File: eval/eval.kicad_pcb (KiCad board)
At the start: 2 copper layers, 2 parts, among them U1 STM32G031G8U6, U2 LM5148RGYR

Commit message: [Layout] complete loop, root and buck layout
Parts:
- added C1: 100n, Capacitor_SMD:C_0603_1608Metric, F.Cu at (77.9, 133.6)
- added C10: 10n, Capacitor_SMD:C_0603_1608Metric, F.Cu at (131.2, 126.4)
- added C11: 10n, Capacitor_SMD:C_0603_1608Metric, F.Cu at (64.9, 175.4)
- added C12: 10n, Capacitor_SMD:C_0603_1608Metric, F.Cu at (135.1, 128.5)
- added C13: 15n, Capacitor_SMD:C_0603_1608Metric, F.Cu at (74.5, 179.3)
- added C14: 100n, Capacitor_SMD:C_0603_1608Metric, F.Cu at (1758.3, 58.4)
- added C15: 15n, Capacitor_SMD:C_0603_1608Metric, F.Cu at (74.5, 176.2)
- added C16: 100n, Capacitor_SMD:C_0603_1608Metric, F.Cu at (1702.5, 61.0)
- added C17: 10n, Capacitor_SMD:C_0603_1608Metric, F.Cu at (69.4, 115.2)
- added C18: 10n, Capacitor_SMD:C_0603_1608Metric, F.Cu at (65.8, 113.5)
- added C19: 1u, Capacitor_SMD:C_0603_1608Metric, F.Cu at (59.2, 84.7)
- added C2: 2.2u, Capacitor_SMD:C_0603_1608Metric, F.Cu at (77.8, 142.0)
- added C20: 4.7u, Capacitor_SMD:C_0603_1608Metric, F.Cu at (59.2, 81.6)
- added C21: 100n, Capacitor_SMD:C_0603_1608Metric, F.Cu at (59.2, 83.1)
- added C22: 100n, Capacitor_SMD:C_0603_1608Metric, F.Cu at (1708.8, 61.0)
- added C23: 22uf, Capacitor_SMD:C_0603_1608Metric, F.Cu at (1790.1, 63.5)
- added C24: 22uf, Capacitor_SMD:C_0603_1608Metric, F.Cu at (1799.0, 63.5)
- added C25: 75p, Capacitor_SMD:C_0603_1608Metric, F.Cu at (1767.2, 73.7)
- added C26: 1u, Capacitor_SMD:C_0603_1608Metric, F.Cu at (1702.5, 121.9)
- added C27: 1u, Capacitor_SMD:C_0603_1608Metric, F.Cu at (1778.7, 121.9)
- added C28: 1u, Capacitor_SMD:C_0603_1608Metric, F.Cu at (1749.4, 123.2)
- added C29: 1u, Capacitor_SMD:C_0603_1608Metric, F.Cu at (1829.5, 123.2)
- added C30: 1u, Capacitor_SMD:C_0603_1608Metric, F.Cu at (1438.6, 119.4)
- added C31: 100p, Capacitor_SMD:C_0603_1608Metric, F.Cu at (1479.3, 142.2)
- added C32: 100p, Capacitor_SMD:C_0603_1608Metric, F.Cu at (1391.6, 128.3)
- added C33: 100, Capacitor_SMD:C_0603_1608Metric, F.Cu at (77.7, 140.5)
- added C36: 10u, EasyEDA:C1206, F.Cu at (88.6, 123.7)
- added C37: 10u, EasyEDA:C1206, F.Cu at (85.2, 123.7)
- added C38: 100n, Capacitor_SMD:C_0603_1608Metric, F.Cu at (64.2, 177.8)
- added C40: 47u, EasyEDA:C1206, F.Cu at (120.3, 140.4)
- added C41: 47u, EasyEDA:C1206, F.Cu at (117.0, 140.4)
- added C42: 47u, EasyEDA:C1206, F.Cu at (113.6, 140.4)
- added C43: 47u, EasyEDA:C1206, F.Cu at (110.3, 140.4)
- added C7: 100n, Capacitor_SMD:C_0603_1608Metric, F.Cu at (75.4, 141.2)
- added C8: 10u, EasyEDA:C1206, F.Cu at (95.2, 123.7)
- added C9: 10u, EasyEDA:C1206, F.Cu at (91.9, 123.7)
- added D1: BAT54,215, EasyEDA:SOT-23_L2.9-W1.3-P1.90-LS2.4-BR, F.Cu at (64.9, 171.6)
- added D2: BDFN2A301V35, EasyEDA:DFN1006-2L-RD, F.Cu at (1134.2, 100.3)
- added D3: BDFN2A301V35, EasyEDA:DFN1006-2L-RD, F.Cu at (1140.5, 100.3)
- added D6: SMAJ20A_C41376408, EasyEDA:SMA_L4.3-W2.6-LS5.2-RD, F.Cu at (1154.5, 100.3)
- added J1: TC2030, Connector:Tag-Connect_TC2030-IDC-NL_2x03_P1.27mm_Vertical, F.Cu at (76.2, 78.0)
- added L1: SMIS130804-R47MT, EasyEDA:IND-SMD_L12.8-W7.8, F.Cu at (99.3, 137.4)
- added Q1: BSC0702LS, EasyEDA:PG-TDSON-8_L5.0-W6.0-P1.27-BL-EP, F.Cu at (86.6, 133.1)
- added Q2: BSC0702LS, EasyEDA:PG-TDSON-8_L5.0-W6.0-P1.27-BL-EP, F.Cu at (86.6, 143.1)
- added Q3: AP40P04G, EasyEDA:PDFN-8_L5.8-W4.9-P1.27-LS6.1-BL-A, F.Cu at (1215.5, 52.1)
- added Q4: DMG2302UK-7, EasyEDA:SOT-23-3_L2.9-W1.3-P1.90-LS2.4-BR, F.Cu at (1410.7, 125.7)
- added R1: RE2512F3R010, EasyEDA:R2512, F.Cu at (69.3, 121.9)
- added R10: R_Small, Resistor_SMD:R_0603_1608Metric, F.Cu at (64.2, 179.3)
- added R11: 10k, Resistor_SMD:R_0603_1608Metric, F.Cu at (61.0, 176.2)
- added R12: 100k, Resistor_SMD:R_0603_1608Metric, F.Cu at (63.3, 175.4)
- added R13: 10, Resistor_SMD:R_0603_1608Metric, F.Cu at (134.2, 130.8)
- added R14: 10, Resistor_SMD:R_0603_1608Metric, F.Cu at (135.9, 130.8)
- added R15: 1k, Resistor_SMD:R_0603_1608Metric, F.Cu at (77.0, 180.1)
- added R16: 49.9, Resistor_SMD:R_0603_1608Metric, F.Cu at (1776.1, 64.8)
- added R17: 100, Resistor_SMD:R_0603_1608Metric, F.Cu at (71.6, 181.4)
- added R18: 1k, Resistor_SMD:R_0603_1608Metric, F.Cu at (76.9, 175.5)
- added R19: 100k, Resistor_SMD:R_0603_1608Metric, F.Cu at (1776.1, 72.4)
- added R2: 100k, Resistor_SMD:R_0603_1608Metric, F.Cu at (73.8, 130.4)
- added R20: 100, Resistor_SMD:R_0603_1608Metric, F.Cu at (71.6, 173.8)
- added R21: 10, Resistor_SMD:R_0603_1608Metric, F.Cu at (68.7, 117.6)
- added R22: 10, Resistor_SMD:R_0603_1608Metric, F.Cu at (70.2, 117.7)
- added R23: 1k, Resistor_SMD:R_0603_1608Metric, F.Cu at (65.8, 111.8)
- added R25: 13.3k, Resistor_SMD:R_0603_1608Metric, F.Cu at (1776.1, 81.3)
- added R26: 22, Resistor_SMD:R_0603_1608Metric, F.Cu at (1149.4, 81.3)
- added R27: 22, Resistor_SMD:R_0603_1608Metric, F.Cu at (1149.4, 83.8)
- added R28: 22, Resistor_SMD:R_0603_1608Metric, F.Cu at (1130.4, 72.4)
- added R29: 22, Resistor_SMD:R_0603_1608Metric, F.Cu at (1130.4, 77.5)
- added R3: 43.2k, Resistor_SMD:R_0603_1608Metric, F.Cu at (72.2, 141.2)
- added R30: 100k, Resistor_SMD:R_0603_1608Metric, F.Cu at (1197.7, 57.1)
- added R31: 10k, Resistor_SMD:R_0603_1608Metric, F.Cu at (1197.7, 64.8)
- added R32: 2.2k, Resistor_SMD:R_0603_1608Metric, F.Cu at (1237.0, 83.8)
- added R33: 2.2k, Resistor_SMD:R_0603_1608Metric, F.Cu at (1233.2, 86.4)
- added R34: 900k, Resistor_SMD:R_0603_1608Metric, F.Cu at (1192.6, 124.5)
- added R35: 900k, Resistor_SMD:R_0603_1608Metric, F.Cu at (1200.2, 124.5)
- added R36: 900k, Resistor_SMD:R_0603_1608Metric, F.Cu at (1196.4, 124.5)
- added R37: 100k, Resistor_SMD:R_0603_1608Metric, F.Cu at (1204.0, 139.7)
- added R38: 100k, Resistor_SMD:R_0603_1608Metric, F.Cu at (1207.8, 139.7)
- added R39: 20, Resistor_SMD:R_0603_1608Metric, F.Cu at (1414.5, 138.4)
- added R4: 10k, Resistor_SMD:R_0603_1608Metric, F.Cu at (75.7, 130.4)
- added R40: 100k, Resistor_SMD:R_0603_1608Metric, F.Cu at (1398.0, 128.3)
- added R41: 72.3k, Resistor_SMD:R_0603_1608Metric, F.Cu at (1448.8, 111.8)
- added R42: 10k, Resistor_SMD:R_0603_1608Metric, F.Cu at (1448.8, 119.4)
- added R43: 330, Resistor_SMD:R_0603_1608Metric, F.Cu at (1490.7, 133.3)
- added R44: 10k, Resistor_SMD:R_0603_1608Metric, F.Cu at (785.3, 63.5)
- added R46: ASR-M-5-0.5F, EasyEDA:R3920, F.Cu at (135.0, 137.0)
- added R5: 29.9k, Resistor_SMD:R_0603_1608Metric, F.Cu at (70.7, 141.2)
- added R6: R_Small, Resistor_SMD:R_0603_1608Metric, F.Cu at (73.4, 148.6)
- added R7: R_Small, Resistor_SMD:R_0603_1608Metric, F.Cu at (73.8, 141.2)
- added R8: 1k, Resistor_SMD:R_0603_1608Metric, F.Cu at (131.2, 124.8)
- added R9: 1k, Resistor_SMD:R_0603_1608Metric, F.Cu at (65.0, 168.4)
- added U1: TPS54302DDCR_C311983, EasyEDA:SOT-23-6_L2.9-W1.6-P0.95-LS2.8-BL, F.Cu at (1743.1, 61.0)
- added U10: TPS7A2033PDBVR, EasyEDA:SOT-23-5_L2.9-W1.6-P0.95-LS2.8-BR, F.Cu at (1730.4, 121.9)
- added U11: RCLAMP0521T-ES, EasyEDA:DFN1006-2L-BI, F.Cu at (1118.9, 99.1)
- added U12: TPS7A2033PDBVR, EasyEDA:SOT-23-5_L2.9-W1.6-P0.95-LS2.8-BR, F.Cu at (1809.1, 121.9)
- added U13: RCLAMP0521T-ES, EasyEDA:DFN1006-2L-BI, F.Cu at (1125.3, 99.1)
- added U14: TLV9061xDBV, Package_TO_SOT_SMD:SOT-23-5, F.Cu at (1472.9, 133.3)
- added U3: INA180A3, Package_TO_SOT_SMD:SOT-23-5, F.Cu at (135.1, 125.6)
- added U4: HUSB238A-BB001-QN16R, EasyEDA:QFN-16_L3.0-W3.0-P0.50-BL-EP1.7, F.Cu at (1202.8, 82.5)
- added U5: TLV9064, Package_SO:TSSOP-14_4.4x5mm_P0.65mm, F.Cu at (69.7, 177.7)
- added U6: HS096T01H13, EasyEDA:LCD-SMD_HS096T01H13, F.Cu at (1428.5, 54.6)
- added U7: TCAN3413DR, EasyEDA:SOP-8_L4.9-W3.9-P1.27-LS6.0-BL-1, F.Cu at (814.5, 57.1)
- added U8: INA180A3, Package_TO_SOT_SMD:SOT-23-5, F.Cu at (69.5, 112.6)
- added U9: STM32G0B1CBTx, Package_QFP:LQFP-48_7x7mm_P0.5mm, F.Cu at (67.7, 84.7)
- added USBC1: TYPE-C-31-M-12, EasyEDA:USB-C_SMD-TYPE-C-31-M-12_1, F.Cu at (1110.0, 77.5)
- moved U1 1697.0 mm to (1743.1, 61.0)
- moved U2 100.6 mm to (74.6, 136.9)
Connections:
- U2 pad 1: unconnected-(U2-NC-Pad1) -> GNDPWR
- U2 pad 10: unconnected-(U2-PGND-Pad10) -> GNDPWR
- U2 pad 11: unconnected-(U2-LO-Pad11) -> Net-(Q2-G)
- U2 pad 12: unconnected-(U2-VIN-Pad12) -> /power/IN_ISNS-
- U2 pad 13: unconnected-(U2-HO-Pad13) -> Net-(Q1-G)
- U2 pad 14: unconnected-(U2-SW-Pad14) -> /power/ISNS+
- U2 pad 15: unconnected-(U2-CBOOT-Pad15) -> Net-(U2-CBOOT)
- U2 pad 16: unconnected-(U2-VCCX-Pad16) -> GNDPWR
- U2 pad 17: unconnected-(U2-PG/SYNCOUT-Pad17) -> /power/PG/SYNCOUT
- U2 pad 18: unconnected-(U2-PFM/SYNC-Pad18) -> /BUCK_SYNC
- U2 pad 19: unconnected-(U2-EN-Pad19) -> /BUCK_EN
- U2 pad 2: unconnected-(U2-NC-Pad2) -> GNDPWR
- U2 pad 20: unconnected-(U2-ISNS+-Pad20) -> /power/ISNS+
- U2 pad 21: unconnected-(U2-VOUT-Pad21) -> /power/OUT_ISNS+
- U2 pad 22: unconnected-(U2-NC-Pad22) -> GNDPWR
- U2 pad 23: unconnected-(U2-NC-Pad23) -> GNDPWR
- U2 pad 24: unconnected-(U2-NC-Pad24) -> GNDPWR
- U2 pad 25: unconnected-(U2-EP-Pad25) -> GNDPWR
- U2 pad 3: unconnected-(U2-CNFG-Pad3) -> Net-(U2-CNFG)
- U2 pad 4: unconnected-(U2-RT-Pad4) -> Net-(U2-RT)
- U2 pad 5: unconnected-(U2-EXTCOMP-Pad5) -> /loop/COMP
- U2 pad 6: unconnected-(U2-FB-Pad6) -> /power/FB
- U2 pad 7: unconnected-(U2-AGND-Pad7) -> GNDA
- U2 pad 8: unconnected-(U2-VDDA-Pad8) -> Net-(U2-VDDA)
- U2 pad 9: unconnected-(U2-VCC-Pad9) -> Net-(U2-VCC)
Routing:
- net /loop/I_CTL_BUFF: track 0.00 -> 5.55 mm
- net /loop/V_CTL_BUFF: track 0.00 -> 5.45 mm
- net Net-(U5A--): track 0.00 -> 5.10 mm
- net Net-(U5C-+): track 0.00 -> 4.62 mm
- net Net-(U5D-+): track 0.00 -> 4.45 mm
- net Net-(D1-C): track 0.00 -> 3.97 mm
- net +5VA: track 0.00 -> 3.48 mm, vias 0 -> 2
- net GNDA: track 0.00 -> 3.44 mm, vias 0 -> 3
- net Net-(U5B--): track 0.00 -> 2.57 mm
- net Net-(U5D--): track 0.00 -> 2.56 mm
- net Net-(U5C--): track 0.00 -> 2.49 mm
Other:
- board outline added: 122.3 x 122.3 mm
- board text added: "LOOP"
- board text added: "Main Sheet"
- board text added: "aux_power_rail"
- board text added: "can"
- board text added: "power"
- board text added: "screen"
- board text added: "usb_pd"

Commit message: [layout] complete for each sub module
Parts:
- removed C24: 22uf, Capacitor_SMD:C_0603_1608Metric
- removed the U1 at (1743.1, 61.0)
- added C3: 100n, Capacitor_SMD:C_0603_1608Metric, F.Cu at (219.1, 113.2)
- added C39: 100n, Capacitor_SMD:C_0603_1608Metric, F.Cu at (122.0, 128.0)
- added C44: 47u, EasyEDA:C1206, F.Cu at (216.3, 31.2)
- added D5: BZX884-B5V6,315, EasyEDA:SOD-882_L1.0-W0.6-RD, F.Cu at (222.7, 96.2)
- added L2: FXL0420-100-M, EasyEDA:IND-SMD_L4.4-W4.2, F.Cu at (209.3, 29.6)
- added R24: 0, Resistor_SMD:R_0603_1608Metric, F.Cu at (225.2, 105.7)
- added R45: 4.22k, Resistor_SMD:R_0603_1608Metric, F.Cu at (122.0, 130.5)
- added R47: 100k, Resistor_SMD:R_0603_1608Metric, F.Cu at (225.2, 107.2)
- moved C29 1621.8 mm to (209.5, 46.8), turned to 90 degrees
- moved U12 1598.7 mm to (212.2, 46.7)
- moved R19 1580.1 mm to (196.8, 25.7), turned to 180 degrees
- moved C23 1576.8 mm to (213.6, 30.2), turned to -90 degrees
- moved R16 1576.6 mm to (199.9, 25.6), turned to 180 degrees
- moved R25 1576.4 mm to (200.6, 29.0), turned to -90 degrees
- moved C25 1571.3 mm to (196.8, 24.1), turned to 0 degrees
- moved C27 1565.0 mm to (215.5, 46.8), turned to -90 degrees
- moved C28 1558.7 mm to (192.7, 46.1), turned to 90 degrees
- moved C14 1554.7 mm to (203.8, 31.9), turned to 0 degrees
- moved U1 1539.6 mm to (203.8, 29.1), turned to 90 degrees
- moved U10 1536.7 mm to (195.5, 46.1)
- moved C26 1505.8 mm to (198.5, 46.1), turned to -90 degrees
- moved C22 1503.2 mm to (206.0, 26.2)
- moved C16 1496.9 mm to (206.0, 24.6)
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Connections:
- U4 pad 11: unconnected-(U4-INT_N-Pad11) -> /usb_pd/INT
- U4 pad 12: unconnected-(U4-EN_N-Pad12) -> Net-(U4-EN_N)
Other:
- board text added: "AUX-BUCK"
- board text added: "PD"
- board text removed: "aux_power_rail"
- board text removed: "can"
- board text removed: "power"
- board text removed: "usb_pd"

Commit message: [layout] trying to put all components in limit dimention
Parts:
- removed U7: TCAN3413DR, EasyEDA:SOP-8_L4.9-W3.9-P1.27-LS6.0-BL-1
- added U15: TCAN1044VDRBRQ1, EasyEDA:VSON-8_L3.0-W3.0-P0.65-BR-EP, F.Cu at (37.9, 87.6)
- moved R44 212.6 mm to (34.5, 87.2), turned to -90 degrees
- moved R18 190.7 mm to (34.8, 127.7), turned to 0 degrees
- moved R15 188.1 mm to (34.8, 123.2), turned to 0 degrees
- moved C15 185.6 mm to (37.3, 127.0), turned to 90 degrees
- moved C13 183.8 mm to (37.3, 123.9), turned to -90 degrees
- moved C44 183.5 mm to (37.3, 71.6), turned to 90 degrees
- moved R20 181.7 mm to (40.2, 129.3), turned to 0 degrees
- moved R17 177.1 mm to (40.1, 121.8), turned to 0 degrees
- moved R34 176.0 mm to (51.3, 77.3), turned to 180 degrees
- moved U5 175.6 mm to (42.1, 125.5), turned to 180 degrees
- moved R9 175.4 mm to (44.4, 133.8), turned to 0 degrees
- moved C27 174.9 mm to (43.4, 78.6), turned to 0 degrees
- moved R35 174.8 mm to (51.4, 75.8), turned to 180 degrees
- moved C23 174.5 mm to (44.4, 72.9), turned to 90 degrees
- moved R32 173.9 mm to (54.0, 78.5), turned to 90 degrees
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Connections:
- R1 pad 1: /power/IN_ISNS+ -> VBUS
- R21 pad 1: /power/IN_ISNS+ -> VBUS
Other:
- board size 122.3 x 122.3 mm -> 41.8 x 90.7 mm
- board text added: "21700"
- board text removed: "AUX-BUCK"
- board text removed: "LOOP"
- board text removed: "Main Sheet"

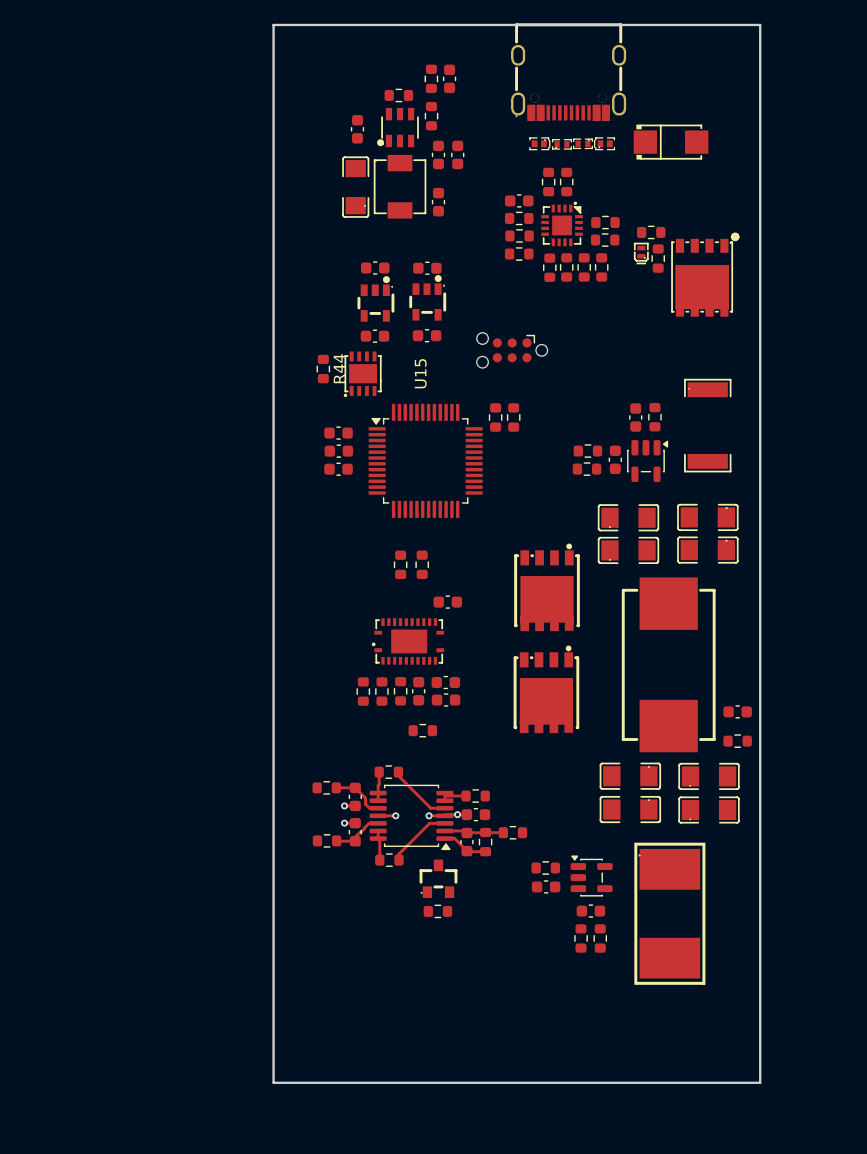
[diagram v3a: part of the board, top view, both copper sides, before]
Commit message: [sch] Add ORing for 2 input
plan to add back to back mos protection for output (high side mos)
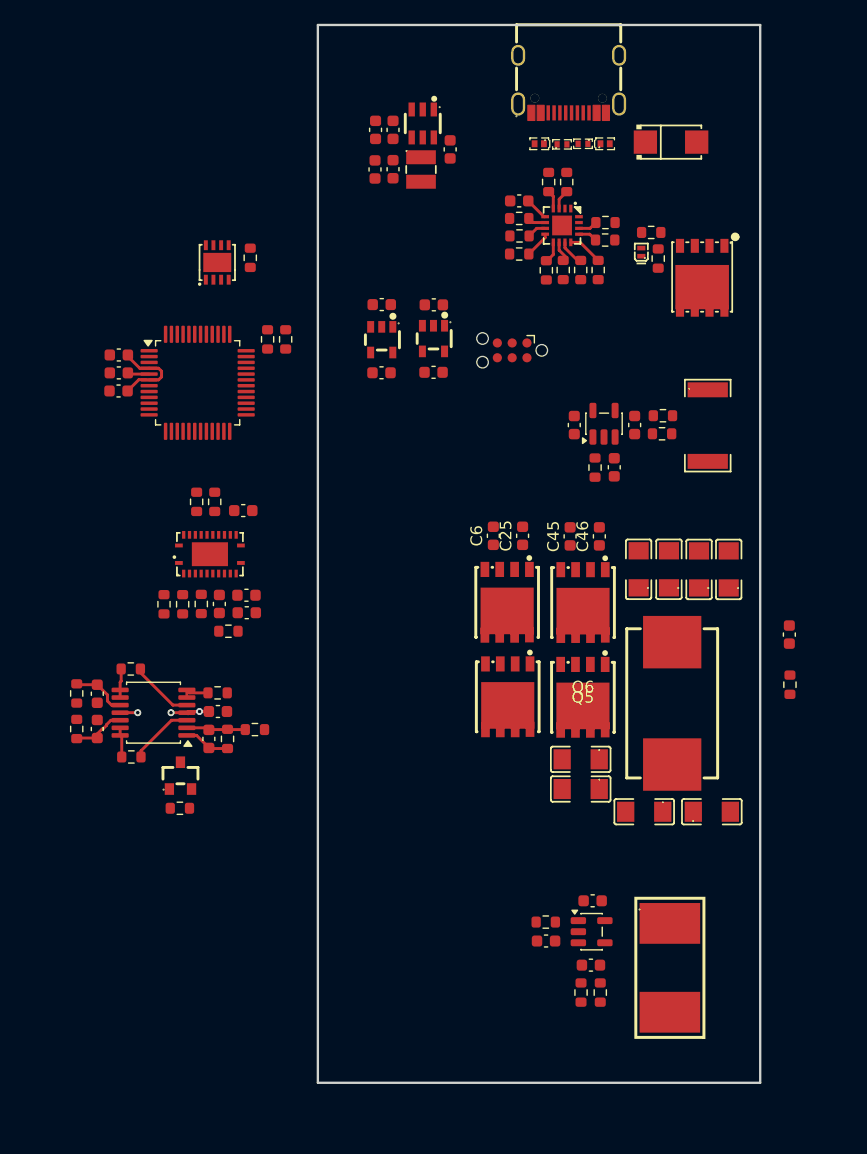
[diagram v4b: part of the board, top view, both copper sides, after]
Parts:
- removed C44: 47u, EasyEDA:C1206
- removed L2: FXL0420-100-M, EasyEDA:IND-SMD_L4.4-W4.2
- removed R16: 49.9, Resistor_SMD:R_0603_1608Metric
- removed R19: 100k, Resistor_SMD:R_0603_1608Metric
- removed R25: 13.3k, Resistor_SMD:R_0603_1608Metric
- added C24: 22uf, Capacitor_SMD:C_0603_1608Metric, F.Cu at (39.0, 70.1)
- added C4: 100n, Capacitor_SMD:C_0603_1608Metric, F.Cu at (57.6, 132.8)
- added C45: 100n, Capacitor_SMD:C_0603_1608Metric, F.Cu at (55.7, 101.6)
- added C46: 100n, Capacitor_SMD:C_0603_1608Metric, F.Cu at (58.2, 101.6)
- added C5: 100n, Capacitor_SMD:C_0603_1608Metric, F.Cu at (56.0, 92.0)
- added C6: 100n, Capacitor_SMD:C_0603_1608Metric, F.Cu at (49.1, 101.5)
- added L3: FTC322512S4R7MBCA, EasyEDA:IND-SMD_L3.2-W2.5_FTC322520S, F.Cu at (42.9, 70.1)
- added Q5: BSC0702LS, EasyEDA:PG-TDSON-8_L5.0-W6.0-P1.27-BL-EP, F.Cu at (56.8, 115.4)
- added Q6: BSC0702LS, EasyEDA:PG-TDSON-8_L5.0-W6.0-P1.27-BL-EP, F.Cu at (56.8, 107.2)
- C25: value 75p -> 100n
- U1: value TPS54302DDCR_C311983 -> AP63205WU-7; footprint EasyEDA:SOT-23-6_L2.9-W1.6-P0.95-LS2.8-BL -> EasyEDA:TSOT-23-6_L2.9-W1.6-P0.95-LS2.8-BL
- moved C25 39.7 mm to (51.6, 101.5), turned to 90 degrees
- moved C15 23.8 mm to (15.1, 118.1)
- moved C38 23.8 mm to (25.5, 116.6)
- moved C13 23.8 mm to (15.1, 115.1)
- moved R11 23.8 mm to (28.6, 118.2)
- moved R17 23.8 mm to (18.0, 113.0)
- moved R9 23.8 mm to (22.2, 124.9)
- moved C11 23.8 mm to (24.7, 119.0)
- moved D1 23.8 mm to (22.3, 122.1)
- moved R10 23.8 mm to (25.4, 115.0)
- moved R12 23.8 mm to (26.3, 119.0)
- moved R20 23.8 mm to (18.1, 120.5)
- moved U5 23.8 mm to (19.9, 116.7)
- moved R18 23.5 mm to (13.4, 118.1), turned to -90 degrees
- moved R15 22.9 mm to (13.4, 115.0), turned to 90 degrees
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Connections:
- net /power/ISNS+ renamed /power/SW
- C25 pad 1: Net-(U1-FB) -> /power/IN_ISNS-
- C25 pad 2: Net-(C25-Pad2) -> GNDPWR
- C38 pad 1: +5VA -> +3V3
- U1 pad 1: GNDA -> +5V
- U1 pad 2: Net-(U1-SW) -> unconnected-(U1-EN-Pad2)
- U1 pad 4: Net-(U1-FB) -> GNDA
- U1 pad 5: unconnected-(U1-EN-Pad5) -> Net-(U1-SW)
- U3 pad 5: +5VA -> +3V3
- U5 pad 4: +5VA -> +3V3
- U8 pad 5: +5VA -> +3V3
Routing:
- net +3V3: track 0.00 -> 13.1 mm, vias 0 -> 2
- net +5VA: track 3.48 -> 0.00 mm, vias 2 -> 0
- net Net-(U4-EN_N): track 0.00 -> 2.99 mm
- net /usb_pd/ORIENT: track 0.00 -> 2.28 mm
- net /usb_pd/INT: track 0.00 -> 2.27 mm
- net GNDA: track 3.44 -> 1.56 mm, vias 3 -> 1
- net Net-(U9-VREF+): track 0.00 -> 1.87 mm
- net Net-(U4-CC1): track 0.00 -> 1.72 mm
- net Net-(U4-FLGIN): track 0.00 -> 1.66 mm
- net Net-(U4-EN_HVDCP/OUT1): track 0.00 -> 1.64 mm
- net /usb_pd/FAULT: track 0.00 -> 1.63 mm
- net Net-(U4-CC2): track 0.00 -> 1.62 mm
- net /I2C_SCL: track 0.00 -> 1.59 mm
- net /usb_pd/DEBUG: track 0.00 -> 1.54 mm
- net /I2C_SDA: track 0.00 -> 1.47 mm
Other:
- board size 41.8 x 90.7 mm -> 38 x 90.7 mm

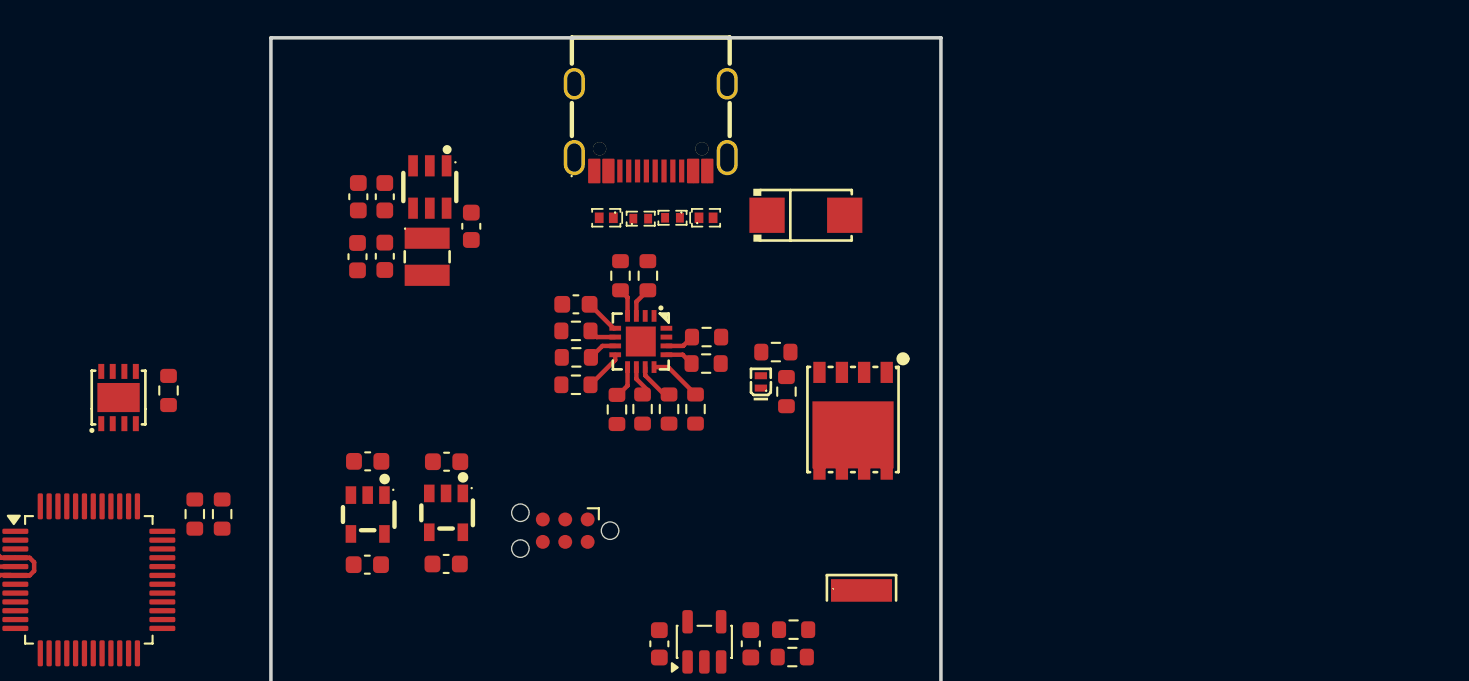
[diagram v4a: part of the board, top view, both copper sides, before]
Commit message: [sch] add back to back protection (MX74502)
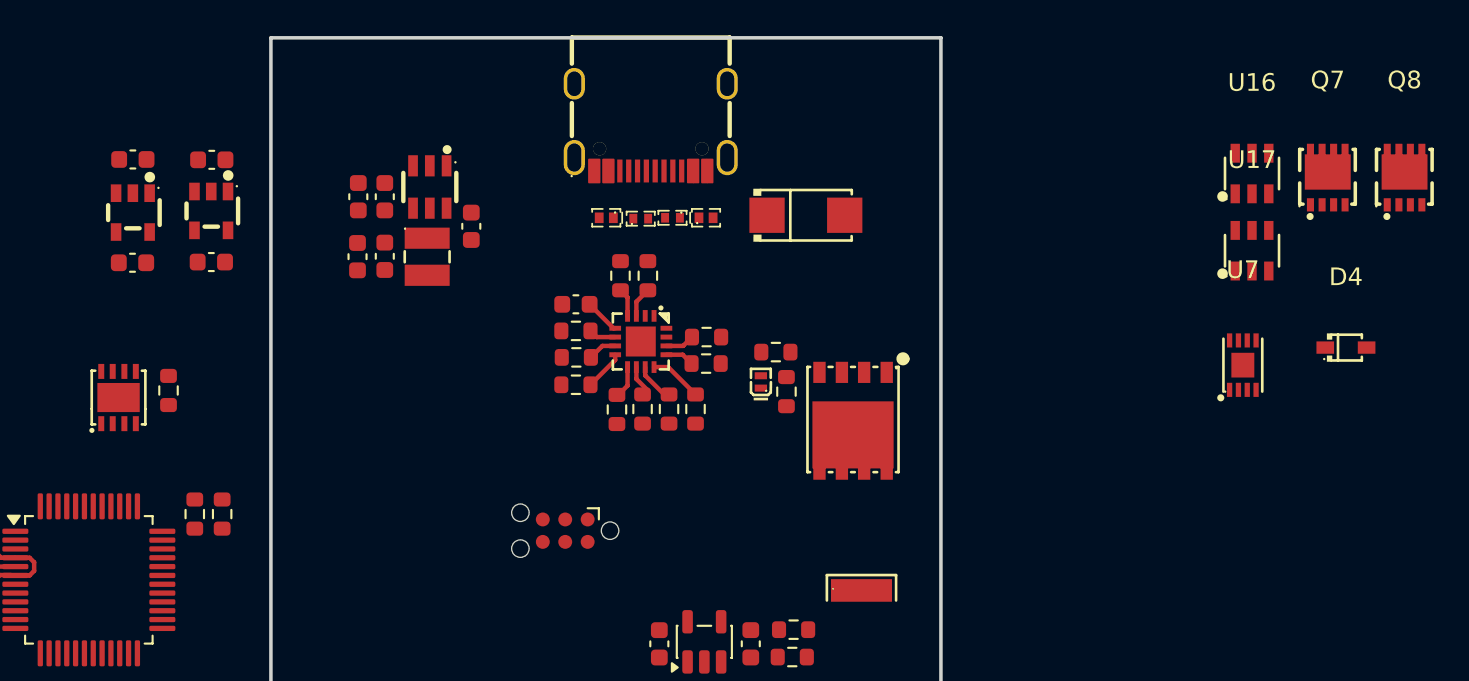
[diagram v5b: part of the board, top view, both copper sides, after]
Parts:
- added D4: BZX384-C12,115, EasyEDA:SOD-323_L1.8-W1.3-LS2.5-RD, F.Cu at (94.9, 75.2)
- added Q7: WSD4070DN, EasyEDA:PDFN3333-8_L3.1-W3.2-P0.65-LS3.4-BL, F.Cu at (93.9, 65.6)
- added Q8: WSD4070DN, EasyEDA:PDFN3333-8_L3.1-W3.2-P0.65-LS3.4-BL, F.Cu at (98.3, 65.6)
- added U16: MX74700T_C22468156, EasyEDA:SOT-23-6_L2.9-W1.6-P0.95-LS2.9-BL, F.Cu at (89.6, 65.4)
- added U17: MX74700T_C22468156, EasyEDA:SOT-23-6_L2.9-W1.6-P0.95-LS2.9-BL, F.Cu at (89.6, 69.8)
- added U7: MX74502D23_C41433189, EasyEDA:UDFN-8L_L2.0-W3.0-P0.50-BL-EP, F.Cu at (89.1, 76.2)
- moved U10 21.7 mm to (26.2, 67.6)
- moved C28 21.7 mm to (26.2, 70.4)
- moved U12 21.7 mm to (30.7, 67.5)
- moved C26 21.7 mm to (26.2, 64.6)
- moved C27 21.7 mm to (30.7, 64.6)
- moved C29 21.7 mm to (30.7, 70.4)
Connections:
- D6 pad 1: Net-(U4-VBUS) -> Net-(D4-K)
- Q3 pad 1: Net-(U4-VBUS) -> Net-(D4-K)
- Q3 pad 2: Net-(U4-VBUS) -> Net-(D4-K)
- Q3 pad 3: Net-(U4-VBUS) -> Net-(D4-K)
- Q3 pad 4: Net-(Q3-G) -> Net-(D4-A)
- Q3 pad 5: VBUS -> /power_mux/INPUT_A
- Q3 pad 6: VBUS -> /power_mux/INPUT_A
- Q3 pad 7: VBUS -> /power_mux/INPUT_A
- Q3 pad 8: VBUS -> /power_mux/INPUT_A
- Q3 pad 9: VBUS -> /power_mux/INPUT_A
- R30 pad 1: Net-(U4-VBUS) -> Net-(D4-K)
- R30 pad 2: Net-(Q3-G) -> Net-(D4-A)
- R31 pad 1: Net-(Q3-G) -> Net-(D4-A)
- U4 pad 16: Net-(U4-VBUS) -> Net-(D4-K)
- USBC1 pad A4B9: Net-(U4-VBUS) -> Net-(D4-K)
- USBC1 pad B4A9: Net-(U4-VBUS) -> Net-(D4-K)
